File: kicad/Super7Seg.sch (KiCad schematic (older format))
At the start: 37 parts, among them IC1 ATMEGA328P-P, P1 UART, Q1 PN2222ABU, Q2 PN2222ABU, Q3 PN2222ABU, Q4 PN2907BU, Q5 PN2907BU, Q6 PN2907BU

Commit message: added footprint mapping
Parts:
- added CON1: AVR-ISP-6, AVR-ISP-6, symbol AVR-ISP-6
- added P2, P3: CONN_01X02, Socket_Strips:Socket_Strip_Straight_1x02, symbol CONN_01X02
- C1, C2, C3: footprint (none) -> Capacitors_ThroughHole:C_Disc_D3_P2.5
- D1, D6: footprint (none) -> footprints:DC08
- D2: renamed from D4; footprint (none) -> footprints:DC08
- D3: renamed from D2; footprint (none) -> footprints:DC08
- D4: renamed from D5; footprint (none) -> footprints:DC08
- D5: renamed from D3; footprint (none) -> footprints:DC08
- IC1: footprint DIL28 -> Housings_DIP:DIP-28_W7.62mm
- P1: footprint (none) -> Socket_Strips:Socket_Strip_Straight_1x06
- Q1, Q6: footprint (none) -> TO_SOT_Packages_THT:TO-92_Inline_Narrow_Oval
- Q2: renamed from Q4; footprint (none) -> TO_SOT_Packages_THT:TO-92_Inline_Narrow_Oval
- Q3: renamed from Q2; footprint (none) -> TO_SOT_Packages_THT:TO-92_Inline_Narrow_Oval
- Q4: renamed from Q5; footprint (none) -> TO_SOT_Packages_THT:TO-92_Inline_Narrow_Oval
- Q5: renamed from Q3; footprint (none) -> TO_SOT_Packages_THT:TO-92_Inline_Narrow_Oval
- R1, R10, R11, R12, R13, R14, R15, R16, R17, R18, R19, R2, R20, R3, R4, R5, R6, R7, R8, R9: footprint (none) -> footprints:0.125_Resistor
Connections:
- net GND: now also CON1.6, P2.1 (P1), P3.1 (P1)
- net PC6: now also CON1.5
- net TX: now also P2.2 (P2), P3.2 (P2)
- net VCC: now also CON1.2
- net MOSI: now reaches IC1.17 ((PCINT3/OC2A/MOSI)PB3), R8.1
- net MOSI: now also CON1.4
- net MISO: now reaches IC1.18 ((PCINT4/MISO)PB4), R9.1
- net MISO: now also CON1.1
- net SCK: now reaches IC1.19 ((PCINT5/SCK)PB5), R10.1
- net SCK: now also CON1.3
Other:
- moved on the sheet: P1

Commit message: more routing work
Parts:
- CON1: footprint AVR-ISP-6 -> footprints:ICSP
- IC1: footprint Housings_DIP:DIP-28_W7.62mm -> footprints:DIP28
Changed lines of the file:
@@
 F 0 "IC1" H 6900 4150 50  0000 L BNN
 F 1 "ATMEGA328P-P" H 8050 1500 50  0000 L BNN
-F 2 "Housings_DIP:DIP-28_W7.62mm" H 7650 2900 50  0001 C CIN
+F 2 "footprints:DIP28" H 7650 2900 50  0001 C CIN
 F 3 "" H 7650 2900 50  0000 C CNN
 	1    7650 2900
@@
 F 0 "CON1" H 6845 5090 50  0000 C CNN
 F 1 "AVR-ISP-6" H 6685 4620 50  0000 L BNN
-F 2 "AVR-ISP-6" V 6430 4890 50  0001 C CNN
+F 2 "footprints:ICSP" V 6430 4890 50  0001 C CNN
 F 3 "" H 6925 4850 50  0000 C CNN
 	1    6950 4850

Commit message: full layout awaiting routing
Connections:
- net RX: now also P2.2 (P2)
- net TX: no longer P2.2 (P2)
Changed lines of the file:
@@
 $EndComp
 Text GLabel 5850 1900 0    50   Input ~ 0
-TX
+RX
 $Comp
 L CONN_01X02 P3

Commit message: new layout plan
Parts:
- removed Q1, Q3, Q5: PN2222ABU, TO_SOT_Packages_THT:TO-92_Inline_Narrow_Oval, symbol Q_NPN_EBC
- removed Q2, Q4, Q6: PN2907BU, TO_SOT_Packages_THT:TO-92_Inline_Narrow_Oval, symbol Q_PNP_EBC
- removed R1, R2, R3: 1.2K, footprints:0.125_Resistor, symbol R
- added P1, P3: CONN_01X13, symbol CONN_01X13
- added P2, P4: CONN_01X09, symbol CONN_01X09
- added QN1, QN2, QN3: PN2222ABU, TO_SOT_Packages_THT:TO-92_Inline_Narrow_Oval, symbol Q_NPN_EBC
- added QP1, QP2, QP3: PN2907BU, TO_SOT_Packages_THT:TO-92_Inline_Narrow_Oval, symbol Q_PNP_EBC
- added R18, R19, R20: 1.2K, footprints:0.125_Resistor, symbol R
- renumbered P1 to P5, P2 to P6, P3 to P7, R9 to R1, R5 to R12, R6 to R13, R18 to R14, R13 to R15, R14 to R16, R4 to R17, R8 to R2, R7 to R3, R12 to R4, R17 to R5, R16 to R6, R19 to R7, R15 to R8, R20 to R9
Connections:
- net A1: now also P1.5 (P5); no longer R12.2
- net A2: now also P1.10 (P10); no longer R15.2
- net B1: now also P1.6 (P6); no longer R13.2
- net B2: now also P1.11 (P11); no longer R16.2
- net C1: now also P2.3 (P3); no longer R3.2
- net C2: now also P2.8 (P8); no longer R8.2
- net D1: now also P2.2 (P2); no longer R2.2
- net D2: now also P2.6 (P6); no longer R6.2
- net DC_1: now also P3.1 (P1), QN1.3 (C); no longer IC1.11 ((PCINT21/OC0B/T1)PD5)
- net DC_2: now also P3.2 (P2), QP1.1 (E); no longer IC1.12 ((PCINT22/OC0A/AIN0)PD6)
- net DC_3: now also P3.7 (P7), QN2.3 (C); no longer IC1.13 ((PCINT23/AIN1)PD7)
- net DP1: now also P2.4 (P4); no longer R4.2
- net DP2: now also P2.9 (P9); no longer R9.2
- net E1: now also P2.1 (P1); no longer R1.2
- net E2: now also P2.5 (P5); no longer R5.2
- net F1: now also P1.3 (P3); no longer R10.2
- net F2: now also P1.9 (P9); no longer R14.2
- net G1: now also P1.4 (P4); no longer R11.2
- net G2: now also P2.7 (P7); no longer R7.2
- net GND: now also QN1.1 (E), QN2.1 (E), QN3.1 (E), QP1.3 (C), QP2.3 (C), QP3.3 (C)
- net DIG1: now reaches D1.13 (C2), D1.14 (C1)
- net DIG1: now also P1.1 (P1)
- net DIG2: now reaches D2.13 (C2), D2.14 (C1)
- net DIG2: now also P1.2 (P2)
- net DIG3: now reaches D3.13 (C2), D3.14 (C1)
- net DIG3: now also P1.7 (P7)
- net DIG4: now reaches D4.13 (C2), D4.14 (C1)
- net DIG4: now also P1.8 (P8)
- net DIG5: now reaches D5.13 (C2), D5.14 (C1)
- net DIG5: now also P1.12 (P12)
- net DIG6: now reaches D6.13 (C2), D6.14 (C1)
- net DIG6: now also P1.13 (P13)
- net DC_A: now reaches IC1.6 ((PCINT20/XCK/T0)PD4)
- net DC_A: now also R18.1
- new net: QN1.2 (B), QP1.2 (B), R18.2
- new net: QN2.2 (B), QP2.2 (B), R19.2
- new net: QN3.2 (B), QP3.2 (B), R20.2
- new net DC_4: P3.8 (P8), QP2.1 (E)
- new net DC_5: P3.12 (P12), QN3.3 (C)
- new net DC_6: P3.13 (P13), QP3.1 (E)
- new net DC_B: IC1.11 ((PCINT21/OC0B/T1)PD5), R19.1
- new net DC_C: IC1.12 ((PCINT22/OC0A/AIN0)PD6), R20.1
- new net H_A1: P3.5 (P5), R12.2
- new net H_A2: P3.10 (P10), R15.2
- new net H_B1: P3.6 (P6), R13.2
- new net H_B2: P3.11 (P11), R16.2
- new net H_C1: P4.3 (P3), R3.2
- new net H_C2: P4.8 (P8), R8.2
- new net H_D1: P4.2 (P2), R2.2
- new net H_D2: P4.6 (P6), R6.2
- new net H_DP1: P4.4 (P4), R4.2
- new net H_DP2: P4.9 (P9), R9.2
- new net H_E1: P4.1 (P1), R1.2
- new net H_E2: P4.5 (P5), R5.2
- new net H_F1: P3.3 (P3), R10.2
- new net H_F2: P3.9 (P9), R14.2
- new net H_G1: P3.4 (P4), R11.2
- new net H_G2: P4.7 (P7), R7.2

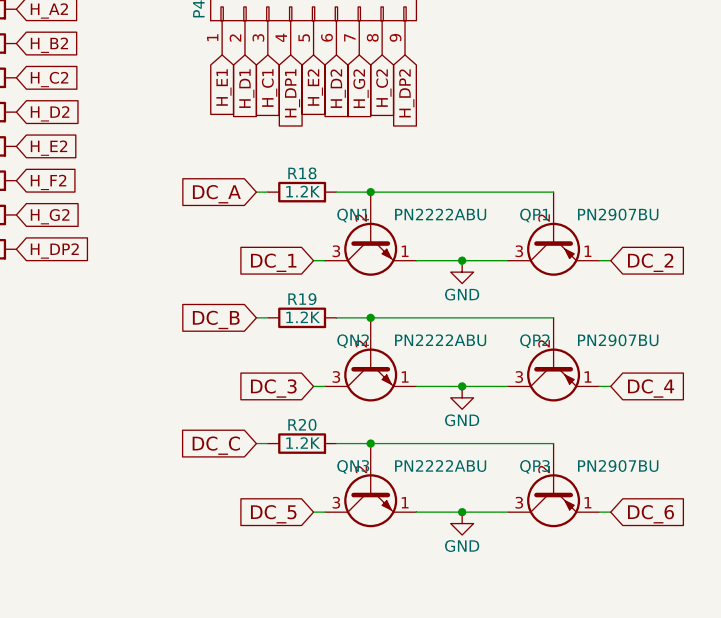
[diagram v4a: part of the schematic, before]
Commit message: added new transistor resistors
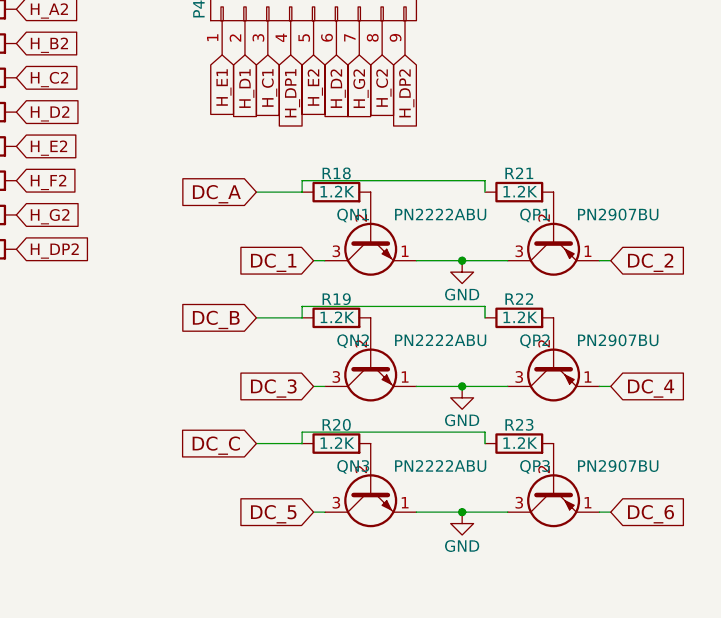
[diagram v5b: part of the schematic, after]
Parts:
- added R21, R22, R23: 1.2K, footprints:0.125_Resistor, symbol R
- P1, P3: footprint (none) -> Socket_Strips:Socket_Strip_Straight_1x13
- P2, P4: footprint (none) -> Socket_Strips:Socket_Strip_Straight_1x09
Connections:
- net DC_A: now also R21.1
- net DC_B: now also R22.1
- net DC_C: now also R23.1
- net at QN1.2 (B), R18.2: no longer QP1.2 (B)
- net at QN2.2 (B), R19.2: no longer QP2.2 (B)
- net at QN3.2 (B), R20.2: no longer QP3.2 (B)
- new net: QP1.2 (B), R21.2
- new net: QP2.2 (B), R22.2
- new net: QP3.2 (B), R23.2
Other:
- moved on the sheet: R18, R19, R20
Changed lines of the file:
@@
 L R R18
 U 1 1 5866B72E
-P 10800 3450
-F 0 "R18" V 10880 3450 50  0000 C CNN
-F 1 "1.2K" V 10800 3450 50  0000 C CNN
-F 2 "footprints:0.125_Resistor" V 10730 3450 50  0001 C CNN
-F 3 "" H 10800 3450 50  0000 C CNN
-	1    10800 3450
+P 10950 3450
+F 0 "R18" V 11030 3450 50  0000 C CNN
+F 1 "1.2K" V 10950 3450 50  0000 C CNN
+F 2 "footprints:0.125_Resistor" V 10880 3450 50  0001 C CNN
+F 3 "" H 10950 3450 50  0000 C CNN
+	1    10950 3450
 	0    -1   -1   0
 $EndComp
@@
 DC_A
 Wire Wire Line
-	10600 3450 10650 3450
-Connection ~ 11100 3450
+	10600 3450 10800 3450
 $Comp
 L GND #PWR017
@@
 	11300 3750 11700 3750
 Connection ~ 11500 3750
-Wire Wire Line
-	10950 3450 11900 3450
 Text GLabel 10850 3750 0    60   Input ~ 0
 DC_1
@@
 L R R19
 U 1 1 5867097F
-P 10800 4000
-F 0 "R19" V 10880 4000 50  0000 C CNN
-F 1 "1.2K" V 10800 4000 50  0000 C CNN
-F 2 "footprints:0.125_Resistor" V 10730 4000 50  0001 C CNN
-F 3 "" H 10800 4000 50  0000 C CNN
-	1    10800 4000
+P 10950 4000
+F 0 "R19" V 11030 4000 50  0000 C CNN
+F 1 "1.2K" V 10950 4000 50  0000 C CNN
+F 2 "footprints:0.125_Resistor" V 10880 4000 50  0001 C CNN
+F 3 "" H 10950 4000 50  0000 C CNN
+	1    10950 4000
 	0    -1   -1   0
 $EndComp
@@
 DC_B
 Wire Wire Line
-	10600 4000 10650 4000
-Connection ~ 11100 4000
+	10600 4000 10800 4000
 $Comp
 L GND #PWR018
@@
 	11300 4300 11700 4300
 Connection ~ 11500 4300
-Wire Wire Line
-	10950 4000 11900 4000
 Text GLabel 10850 4300 0    60   Input ~ 0
 DC_3
@@
 L R R20
 U 1 1 58670A3C
-P 10800 4550
-F 0 "R20" V 10880 4550 50  0000 C CNN
-F 1 "1.2K" V 10800 4550 50  0000 C CNN
-F 2 "footprints:0.125_Resistor" V 10730 4550 50  0001 C CNN
-F 3 "" H 10800 4550 50  0000 C CNN
-	1    10800 4550
+P 10950 4550
+F 0 "R20" V 11030 4550 50  0000 C CNN
+F 1 "1.2K" V 10950 4550 50  0000 C CNN
+F 2 "footprints:0.125_Resistor" V 10880 4550 50  0001 C CNN
+F 3 "" H 10950 4550 50  0000 C CNN
+	1    10950 4550
 	0    -1   -1   0
 $EndComp
@@
 DC_C
 Wire Wire Line
-	10600 4550 10650 4550
-Connection ~ 11100 4550
+	10600 4550 10800 4550
 $Comp
 L GND #PWR019
@@
 	11300 4850 11700 4850
 Connection ~ 11500 4850
-Wire Wire Line
-	10950 4550 11900 4550
 Text GLabel 10850 4850 0    60   Input ~ 0
 DC_5
@@
 F 0 "P3" H 10850 3050 50  0000 C CNN
 F 1 "CONN_01X13" V 10950 2350 50  0000 C CNN
-F 2 "" H 10850 2350 50  0000 C CNN
+F 2 "Socket_Strips:Socket_Strip_Straight_1x13" H 10850 2350 50  0001 C CNN
 F 3 "" H 10850 2350 50  0000 C CNN
 	1    10850 2350
@@
 F 0 "P4" H 10850 3150 50  0000 C CNN
 F 1 "CONN_01X09" V 10950 2650 50  0000 C CNN
-F 2 "" H 10850 2650 50  0000 C CNN
+F 2 "Socket_Strips:Socket_Strip_Straight_1x09" H 10850 2650 50  0001 C CNN
 F 3 "" H 10850 2650 50  0000 C CNN
 	1    10850 2650
@@
 F 0 "P1" H 3050 6900 50  0000 C CNN
 F 1 "CONN_01X13" V 3150 6200 50  0000 C CNN
-F 2 "" H 3050 6200 50  0000 C CNN
+F 2 "Socket_Strips:Socket_Strip_Straight_1x13" H 3050 6200 50  0001 C CNN
 F 3 "" H 3050 6200 50  0000 C CNN
 	1    3050 6200
@@
 F 0 "P2" H 3050 7000 50  0000 C CNN
 F 1 "CONN_01X09" V 3150 6500 50  0000 C CNN
-F 2 "" H 3050 6500 50  0000 C CNN
+F 2 "Socket_Strips:Socket_Strip_Straight_1x09" H 3050 6500 50  0001 C CNN
 F 3 "" H 3050 6500 50  0000 C CNN
 	1    3050 6500
@@
 $EndComp
 NoConn ~ 8650 4100
+$Comp
+L R R21
+U 1 1 5868A148
+P 11750 3450
+F 0 "R21" V 11830 3450 50  0000 C CNN
+F 1 "1.2K" V 11750 3450 50  0000 C CNN
+F 2 "footprints:0.125_Resistor" V 11680 3450 50  0001 C CNN
+F 3 "" H 11750 3450 50  0000 C CNN
+	1    11750 3450
+	0    -1   -1   0
+$EndComp
+$Comp
+L R R22
+U 1 1 5868A3CE
+P 11750 4000
+F 0 "R22" V 11830 4000 50  0000 C CNN
+F 1 "1.2K" V 11750 4000 50  0000 C CNN
+F 2 "footprints:0.125_Resistor" V 11680 4000 50  0001 C CNN
+F 3 "" H 11750 4000 50  0000 C CNN
+	1    11750 4000
+	0    -1   -1   0
+$EndComp
+$Comp
+L R R23
+U 1 1 5868A516
+P 11750 4550
+F 0 "R23" V 11830 4550 50  0000 C CNN
+F 1 "1.2K" V 11750 4550 50  0000 C CNN
+F 2 "footprints:0.125_Resistor" V 11680 4550 50  0001 C CNN
+F 3 "" H 11750 4550 50  0000 C CNN
+	1    11750 4550
+	0    -1   -1   0
+$EndComp
+Wire Wire Line
+	10800 4550 10800 4500
+Wire Wire Line
+	10800 4500 11600 4500
+Wire Wire Line
+	11600 4500 11600 4550
+Wire Wire Line
+	10800 4000 10800 3950
+Wire Wire Line
+	10800 3950 11600 3950
+Wire Wire Line
+	11600 3950 11600 4000
+Wire Wire Line
+	10800 3450 10800 3400
+Wire Wire Line
+	10800 3400 11600 3400
+Wire Wire Line
+	11600 3400 11600 3450
 $EndSCHEMATC

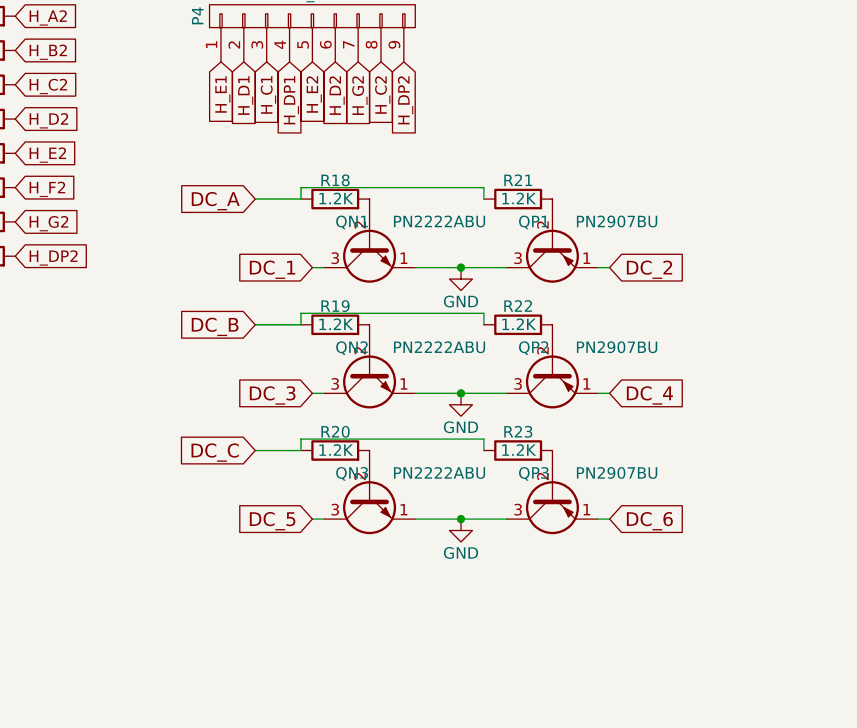
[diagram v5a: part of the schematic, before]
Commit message: Now using ULN2003 and 74HC238
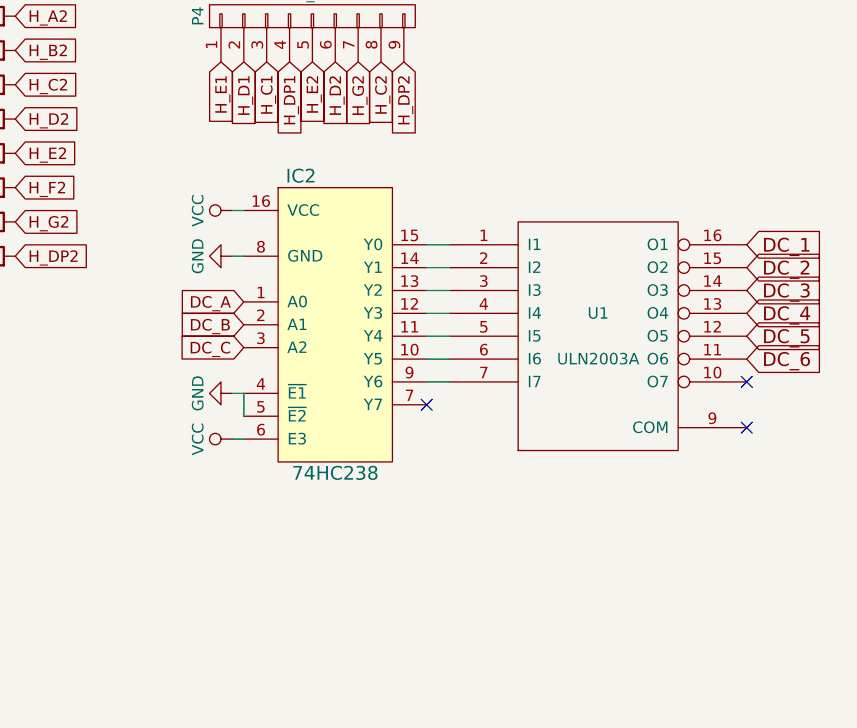
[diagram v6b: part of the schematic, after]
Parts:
- removed QN1, QN2, QN3: PN2222ABU, TO_SOT_Packages_THT:TO-92_Inline_Narrow_Oval, symbol Q_NPN_EBC
- removed QP1, QP2, QP3: PN2907BU, TO_SOT_Packages_THT:TO-92_Inline_Narrow_Oval, symbol Q_PNP_EBC
- removed R18, R19, R20, R21, R22, R23: 1.2K, footprints:0.125_Resistor, symbol R
- added IC2: 74HC238, symbol 74HC238
- added U1: ULN2003A, symbol ULN2003A
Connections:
- net DC_1: now also U1.16 (O1)
- net DC_2: now also U1.15 (O2)
- net DC_3: now also U1.14 (O3)
- net DC_4: now also U1.13 (O4)
- net DC_5: now also U1.12 (O5)
- net DC_6: now also U1.11 (O6)
- net DC_A: now also IC2.1 (A0)
- net DC_B: now also IC2.2 (A1)
- net DC_C: now also IC2.3 (A2)
- net GND: now also IC2.4 (~E1~), IC2.5 (~E2~), IC2.8 (GND), U1.8 (GND)
- net VCC: now also IC2.16 (VCC), IC2.6 (E3)
- new net: IC2.15 (Y0), U1.1 (I1)
- new net: IC2.14 (Y1), U1.2 (I2)
- new net: IC2.13 (Y2), U1.3 (I3)
- new net: IC2.12 (Y3), U1.4 (I4)
- new net: IC2.11 (Y4), U1.5 (I5)
- new net: IC2.10 (Y5), U1.6 (I6)
- new net: IC2.9 (Y6), U1.7 (I7)
- no-connect marks 2 -> 5

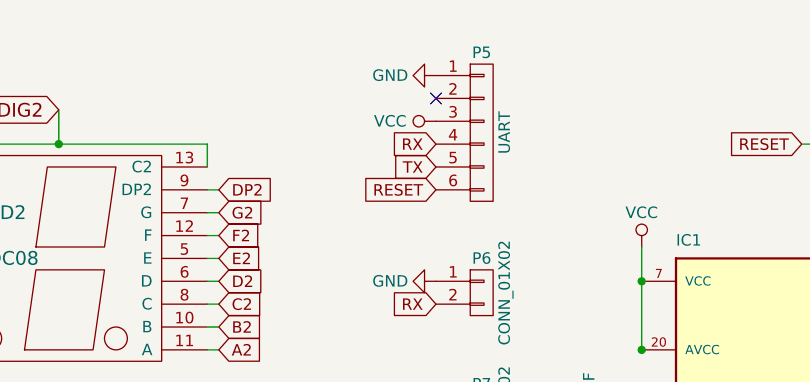
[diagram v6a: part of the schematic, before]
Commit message: Grounded CTS
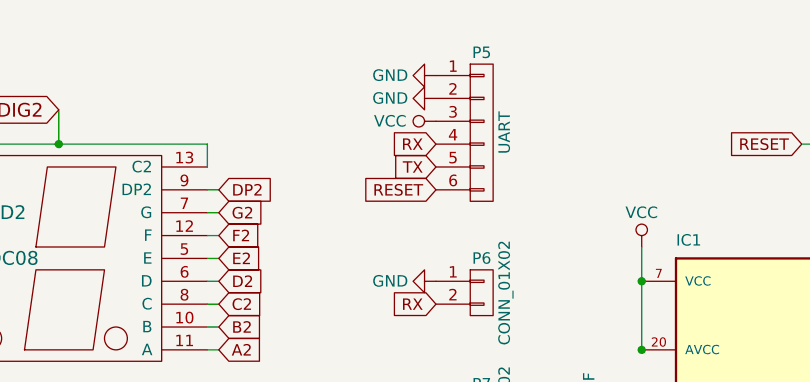
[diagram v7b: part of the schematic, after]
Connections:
- net GND: now also P5.2 (P2)
- no-connect marks 5 -> 4
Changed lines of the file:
@@
 Text GLabel 5850 1200 0    50   Input ~ 0
 RX
-NoConn ~ 5850 1000
 $Comp
 L VCC #PWR05
@@
 Text GLabel 10550 4100 0    50   Input ~ 0
 DC_C
+$Comp
+L GND #PWR?
+U 1 1 5871A688
+P 5850 1000
+F 0 "#PWR?" H 5850 750 50  0001 C CNN
+F 1 "GND" V 5850 800 50  0000 C CNN
+F 2 "" H 5850 1000 50  0000 C CNN
+F 3 "" H 5850 1000 50  0000 C CNN
+	1    5850 1000
+	0    1    -1   0
+$EndComp
 $EndSCHEMATC
